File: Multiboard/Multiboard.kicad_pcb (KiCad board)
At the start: 2 copper layers, 120 x 120 mm, 104 parts, among them J1 Conn_01x20_Socket, J2 Conn_01x20_Socket, J3 Debug, J4 USB_C_Receptacle_USB2.0_16P, Q1 Q_Dual_NMOS_G1S2G2D2S1D1, Q14 Q_Dual_NMOS_G1S2G2D2S1D1, Q2 Q_Dual_NMOS_G1S2G2D2S1D1, Q3 Q_Dual_NMOS_G1S2G2D2S1D1, Q4 Q_Dual_NMOS_G1S2G2D2S1D1, Q5 Q_Dual_NMOS_G1S2G2D2S1D1, Q6 Q_Dual_NMOS_G1S2G2D2S1D1, Q7 Q_Dual_NMOS_G1S2G2D2S1D1, SW1 BOOT0, SW2 NRST, SW3 SW_SPST, SW4 SW_SPST, SW5 SW_SPST, SW7 SW_SPST, SW8 KEY, SW9 SW_SPST, U1 STM32F411RET6, U2 MAX662AESA_T, U3 MCP1792x-3302xCB, U4 USART1, U5 I2C1, U6 SPI1, U7 ADC, U8 GPIO-PWM, Y1 32.768KHz, Y2 25MHz

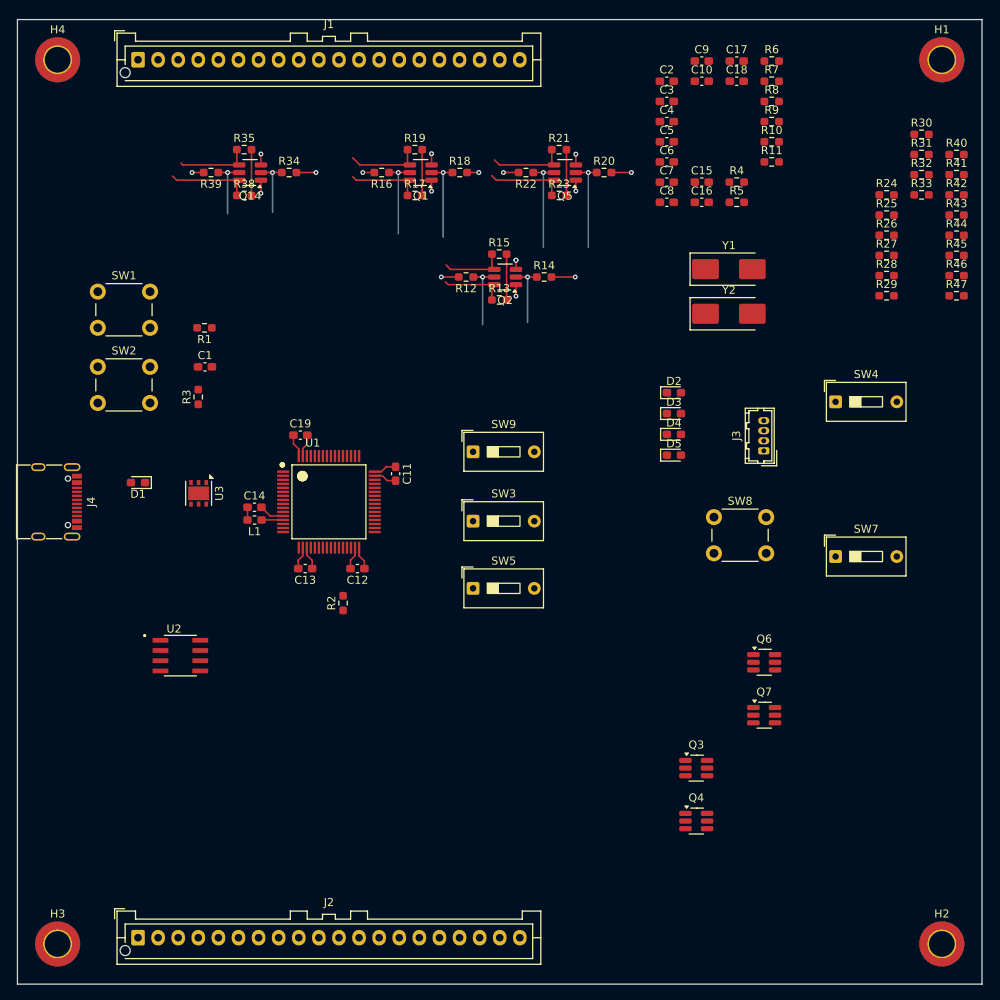
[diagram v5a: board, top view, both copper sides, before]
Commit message: wired all level shifters and increased width of decoupling traces
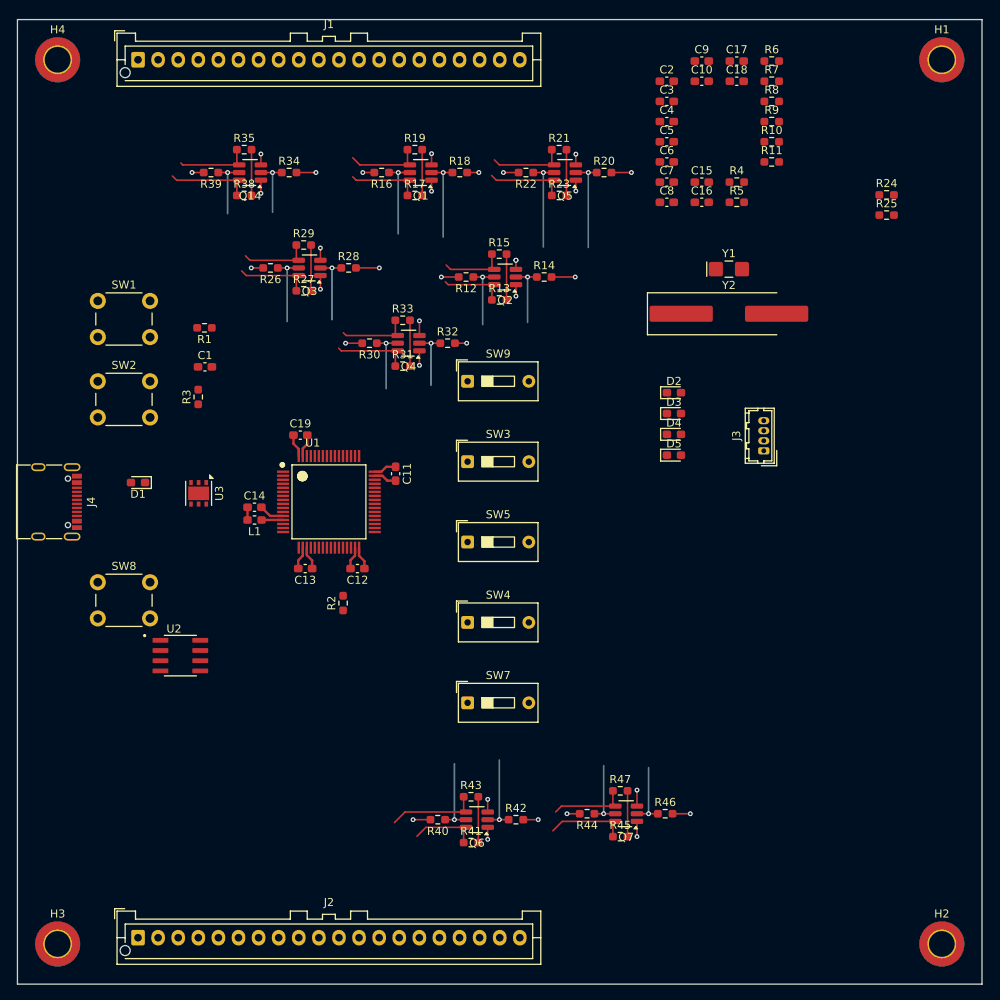
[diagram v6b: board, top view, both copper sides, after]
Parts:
- removed U4: USART1, Level_Shifter:Level_Shifter_3_CH
- removed U5: I2C1, Level_Shifter:Level_Shifter_3_CH
- removed U6: SPI1, Level_Shifter:Level_Shifter_3_CH
- removed U7: ADC, Level_Shifter:Level_Shifter_3_CH
- removed U8: GPIO-PWM, Level_Shifter:Level_Shifter_3_CH
- Y1: footprint Crystal:Crystal_SMD_0603-2Pin_6.0x3.5mm_HandSoldering -> Crystal:Crystal_SMD_MicroCrystal_CC7V-T1A-2Pin_3.2x1.5mm_HandSoldering
- Y2: footprint Crystal:Crystal_SMD_0603-2Pin_6.0x3.5mm_HandSoldering -> Crystal:Crystal_SMD_HC49-SD_HandSoldering
- moved R40 104.9 mm to (92.3, 139.5), turned to 180 degrees
- moved R41 102.7 mm to (96.4, 142.4)
- moved R42 95.1 mm to (102.0, 139.5)
- moved R43 94.3 mm to (96.4, 136.7)
- moved R44 85.4 mm to (110.9, 138.8), turned to 180 degrees
- moved R45 83.5 mm to (115.0, 141.7)
- moved Q3 78.7 mm to (76.3, 70.9), turned to 180 degrees
- moved SW8 77.1 mm to (50.0, 110.0)
- moved R26 76.8 mm to (71.5, 70.9), turned to 180 degrees
- moved R46 76.1 mm to (120.6, 138.8)
- moved R47 74.5 mm to (115.0, 135.9)
- moved R30 73.4 mm to (83.8, 80.3), turned to 180 degrees
- moved R29 72.8 mm to (75.6, 68.0)
- moved R27 72.7 mm to (75.6, 73.7)
- moved R31 69.7 mm to (87.9, 83.1)
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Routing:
- net 3V3: track 38.9 -> 68.5 mm, vias 17 -> 33
- net PC7-GPIO: track 0.00 -> 11.5 mm
- net Net-(SW4-B): track 0.00 -> 11.4 mm
- net Net-(SW7-B): track 0.00 -> 11.4 mm
- net PC8-GPIO: track 0.00 -> 10.3 mm
- net PC7-MCU: track 0.00 -> 10.0 mm, vias 0 -> 1
- net PC9-GPIO: track 0.00 -> 9.75 mm
- net PC6-MCU: track 0.00 -> 9.55 mm, vias 0 -> 1
- net PA6-GPIO: track 0.00 -> 9.51 mm
- net PA4-GPIO: track 0.00 -> 9.37 mm
- net PA4-MCU: track 0.00 -> 9.27 mm, vias 0 -> 1
- net PA5-MCU: track 0.00 -> 9.05 mm, vias 0 -> 1
- net PA7-GPIO: track 0.00 -> 8.93 mm
- net PA5-GPIO: track 0.00 -> 8.88 mm
- net PC6-GPIO: track 0.00 -> 8.59 mm
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
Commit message: wired level shifters; positioed ldo and charge pump
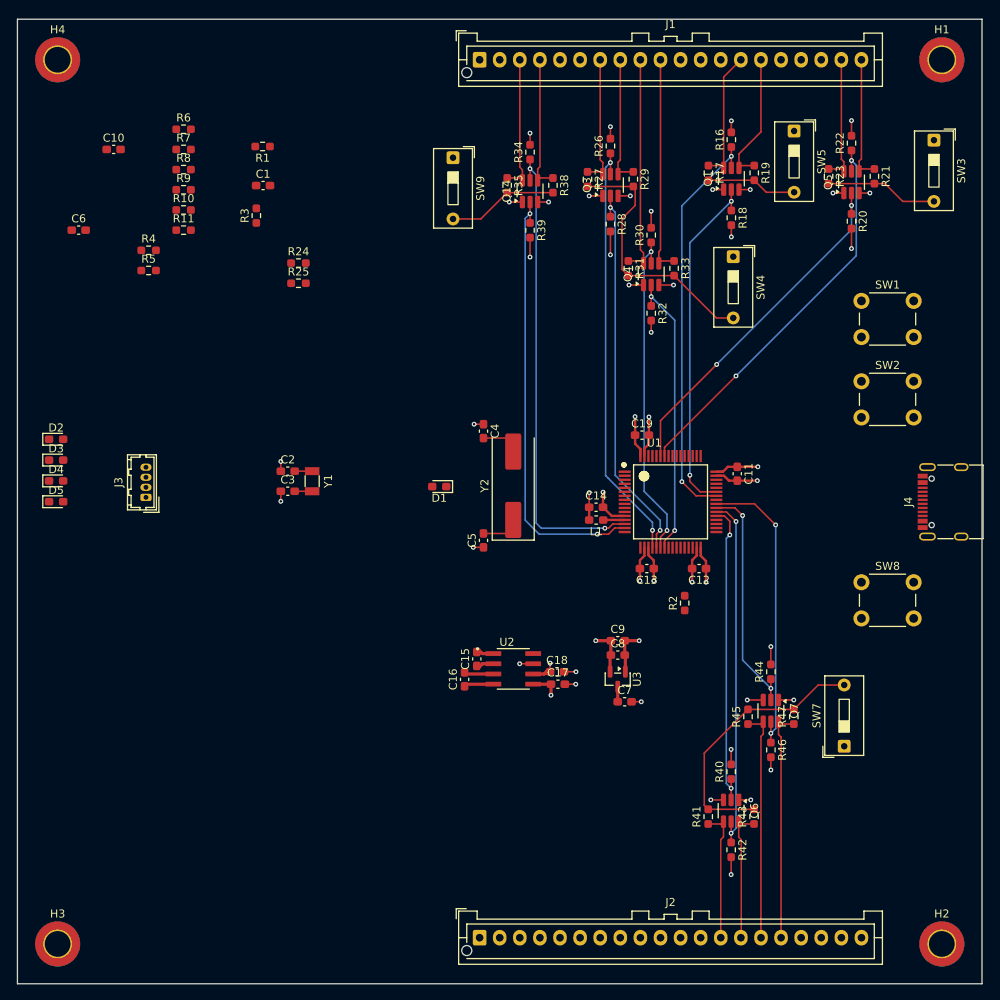
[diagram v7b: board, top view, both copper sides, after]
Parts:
- removed Q2: Q_Dual_NMOS_G1S2G2D2S1D1, Package_TO_SOT_SMD:SOT-23-6_Handsoldering
- removed R12, R13, R14, R15: 10k, Resistor_SMD:R_0603_1608Metric_Pad0.98x0.95mm_HandSolder
- U3: footprint Package_DFN_QFN:DFN-6-1EP_3x3mm_P0.95mm_EP1.7x2.6mm -> Package_TO_SOT_SMD:SOT-23
- Y1: footprint Crystal:Crystal_SMD_MicroCrystal_CC7V-T1A-2Pin_3.2x1.5mm_HandSoldering -> Crystal:Crystal_SMD_3215-2Pin_3.2x1.5mm
- Y2: footprint Crystal:Crystal_SMD_HC49-SD_HandSoldering -> Crystal:Crystal_SMD_HC49-SD
- moved J4 112.7 mm to (156.3, 100.0), turned to 90 degrees
- moved SW1 95.0 mm to (145.0, 75.0)
- moved SW2 95.0 mm to (145.0, 85.0)
- moved SW8 95.0 mm to (145.0, 110.0)
- moved C17 80.7 mm to (107.2, 122.7)
- moved D2 77.1 mm to (44.8, 92.2)
- moved D3 77.1 mm to (44.8, 94.8)
- moved D4 77.1 mm to (44.8, 97.4)
- moved D5 77.1 mm to (44.8, 100.0)
- moved J3 77.1 mm to (56.0, 99.4)
- moved C18 76.8 mm to (107.1, 121.1)
- moved R10 73.7 mm to (60.7, 63.7)
- moved R11 73.7 mm to (60.7, 66.2)
- moved R4 73.7 mm to (56.3, 68.7)
- moved R5 73.7 mm to (56.3, 71.2)
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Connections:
- J1 pad 16: PA11-GPIO -> /PC10
- J1 pad 17: PA12-GPIO -> /PC11
- Q14 pad 2: PA0-MCU -> PA1-MCU
- Q14 pad 4: PA0-GPIO -> PA1-GPIO
- Q14 pad 5: PA1-MCU -> PA0-MCU
- Q14 pad 6: PA1-GPIO -> PA0-GPIO
- Q6 pad 2: PC7-MCU -> PC6-MCU
- Q6 pad 4: PC7-GPIO -> PC6-GPIO
- Q6 pad 5: PC6-MCU -> PC7-MCU
- Q6 pad 6: PC6-GPIO -> PC7-GPIO
- Q7 pad 2: PC9-MCU -> PC8-MCU
- Q7 pad 4: PC9-GPIO -> PC8-GPIO
- Q7 pad 5: PC8-MCU -> PC9-MCU
- Q7 pad 6: PC8-GPIO -> PC9-GPIO
- U1 pad 44: PA11-MCU -> unconnected-(U1-PA11-Pad44)
- U1 pad 45: PA12-MCU -> unconnected-(U1-PA12-Pad45)
- U1 pad 51: unconnected-(U1-PC10-Pad51) -> /PC10
- U1 pad 52: unconnected-(U1-PC11-Pad52) -> /PC11
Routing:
- net PA0-MCU: track 7.54 -> 58.5 mm, vias 1 -> 2
- net PA1-MCU: track 7.72 -> 54.4 mm, vias 1 -> 2
- net PA4-MCU: track 9.27 -> 53.2 mm, vias 1 -> 2
- net PA9-MCU: track 10.2 -> 50.6 mm, vias 1 -> 2
- net PA5-MCU: track 9.05 -> 47.7 mm, vias 1 -> 2
- net PB6-MCU: track 11.9 -> 49.5 mm, vias 1 -> 2
- net PC7-MCU: track 10.0 -> 44.6 mm, vias 1 -> 2
- net PA6-MCU: track 8.25 -> 41.3 mm, vias 1 -> 2
- net PA10-MCU: track 10.6 -> 43.4 mm, vias 1 -> 2
- net PB7-MCU: track 11.9 -> 43.6 mm, vias 1 -> 2
- net PC9-MCU: track 8.34 -> 37.2 mm, vias 1 -> 2
- net PC6-MCU: track 9.55 -> 38.2 mm, vias 1 -> 2
- net PA7-MCU: track 7.85 -> 35.6 mm, vias 1 -> 2
- net GND: track 14.5 -> 40.7 mm, vias 0 -> 14
- net Net-(SW7-B): track 11.4 -> 33.8 mm
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
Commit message: positioned and wired ldo charge pump buttons leds and rtc circuit
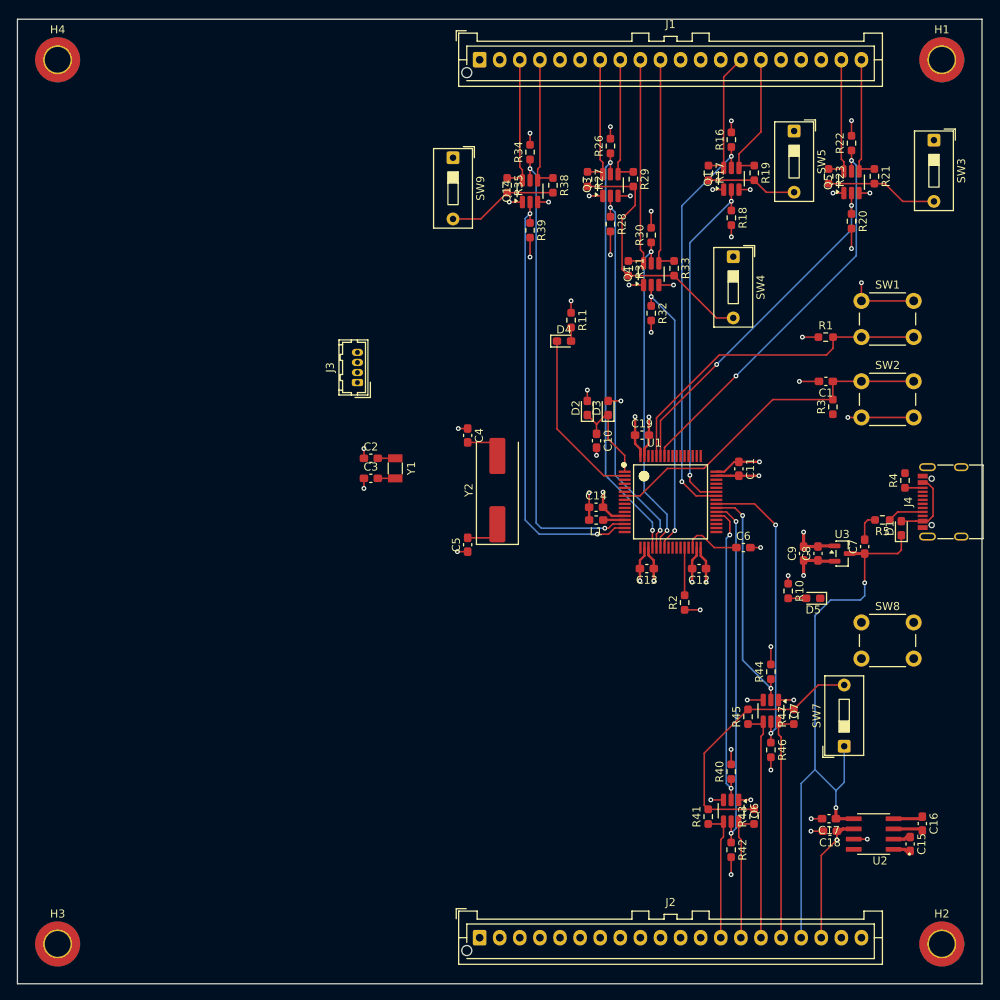
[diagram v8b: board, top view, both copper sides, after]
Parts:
- removed R24, R25: 10k, Resistor_SMD:R_0603_1608Metric_Pad0.98x0.95mm_HandSolder
- removed R6, R7, R8, R9: 10, Resistor_SMD:R_0603_1608Metric_Pad0.98x0.95mm_HandSolder
- moved R4 98.4 mm to (150.4, 97.3), turned to 90 degrees
- moved R5 96.4 mm to (147.6, 102.2), turned to 180 degrees
- moved D5 94.9 mm to (139.0, 112.0), turned to 180 degrees
- moved C6 91.6 mm to (130.3, 105.7)
- moved R10 88.9 mm to (135.9, 111.1), turned to -90 degrees
- moved R3 75.6 mm to (141.4, 88.2)
- moved C1 74.1 mm to (140.6, 85.0), turned to 180 degrees
- moved R1 74.0 mm to (140.6, 79.5), turned to 0 degrees
- moved C10 70.2 mm to (112.0, 92.4), turned to -90 degrees
- moved D3 69.0 mm to (113.5, 88.3), turned to 90 degrees
- moved D2 66.2 mm to (110.9, 88.3), turned to 90 degrees
- moved D4 65.5 mm to (108.0, 80.0)
- moved C16 59.7 mm to (152.6, 140.0), turned to -90 degrees
- moved C15 58.6 mm to (151.1, 142.6), turned to -90 degrees
- moved D1 57.7 mm to (150.0, 103.3), turned to 90 degrees
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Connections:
- U1 pad 44: unconnected-(U1-PA11-Pad44) -> /D-
- U1 pad 45: unconnected-(U1-PA12-Pad45) -> /D+
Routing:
- net 5V: track 5.45 -> 77.0 mm, vias 1 -> 2
- net Net-(U1-NRST): track 0.03 -> 43.2 mm
- net Net-(U1-BOOT0): track 0.00 -> 41.7 mm
- net /PC13: track 0.00 -> 21.8 mm
- net GND: track 40.7 -> 59.8 mm, vias 14 -> 19
- net 3V3: track 74.6 -> 88.3 mm, vias 33 -> 37
- net 12V: track 3.28 -> 16.3 mm
- net Net-(D2-K): track 0.00 -> 12.6 mm
- net Net-(D1-A): track 0.00 -> 9.23 mm
- net Net-(U1-VCAP1): track 0.00 -> 7.28 mm
- net Net-(U1-PB2): track 0.01 -> 5.92 mm
- net Net-(J4-CC1): track 0.00 -> 4.51 mm
- net Net-(D5-A): track 0.00 -> 2.24 mm
- net Net-(J4-CC2): track 0.00 -> 2.20 mm
- net Net-(D4-A): track 0.00 -> 1.69 mm
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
